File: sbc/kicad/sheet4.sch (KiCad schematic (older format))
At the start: 44 parts, among them SW1 \"D\", SW10 \"4\", SW11 \"5\", SW12 \"6\", SW13 \"1\", SW14 \"2\", SW15 \"3\", SW16 \"0\", SW17 \"RESET\", SW18 SEGMENT TEST, SW2 \"E\", SW3 \"F\", SW4 \"A\", SW5 \"B\", SW6 \"C\", SW7 \"7\", SW8 \"8\", SW9 \"9\", U10 MAN71A, U11 74LS259, U12 74LS259, U13 74LS259, U14 74LS259, U15 74LS259, U16 74LS259, U17 74LS244, U5 MAN71A, U6 MAN71A, U7 MAN71A, U8 MAN71A, U9 MAN71A

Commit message: Updates, start of PCB.
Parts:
- removed SW18: SEGMENT TEST, symbol Switch:SW_Push_45deg
- added J11: SEGMENT TEST, Connector_PinHeader_2.54mm:PinHeader_1x02_P2.54mm_Vertical, symbol Connector:Conn_01x02_Male
- C23: footprint (none) -> Capacitor_THT:CP_Radial_D4.0mm_P2.00mm
- R5: renamed from R53; footprint (none) -> Resistor_THT:R_Axial_DIN0204_L3.6mm_D1.6mm_P7.62mm_Horizontal
- R6: renamed from R54; footprint (none) -> Resistor_THT:R_Axial_DIN0204_L3.6mm_D1.6mm_P7.62mm_Horizontal
- RN1: renamed from RN3; footprint (none) -> Connector_PinHeader_2.54mm:PinHeader_2x08_P2.54mm_Vertical
- RN2: renamed from RN4; footprint (none) -> Connector_PinHeader_2.54mm:PinHeader_2x08_P2.54mm_Vertical
- RN3: renamed from RN5; footprint (none) -> Connector_PinHeader_2.54mm:PinHeader_2x08_P2.54mm_Vertical
- RN4: renamed from RN6; footprint (none) -> Connector_PinHeader_2.54mm:PinHeader_2x08_P2.54mm_Vertical
- RN5: renamed from RN7; footprint (none) -> Connector_PinHeader_2.54mm:PinHeader_2x08_P2.54mm_Vertical
- RN6: renamed from RN8; footprint (none) -> Connector_PinHeader_2.54mm:PinHeader_2x08_P2.54mm_Vertical
- SW10: renamed from SW9; footprint (none) -> Button_Switch_THT:SW_PUSH_6mm_H4.3mm
- SW11: renamed from SW10; footprint (none) -> Button_Switch_THT:SW_PUSH_6mm_H4.3mm
- SW12: renamed from SW11; footprint (none) -> Button_Switch_THT:SW_PUSH_6mm_H4.3mm
- SW13: renamed from SW12; footprint (none) -> Button_Switch_THT:SW_PUSH_6mm_H4.3mm
- SW14: renamed from SW13; footprint (none) -> Button_Switch_THT:SW_PUSH_6mm_H4.3mm
- SW15: renamed from SW14; footprint (none) -> Button_Switch_THT:SW_PUSH_6mm_H4.3mm
- SW16: renamed from SW15; footprint (none) -> Button_Switch_THT:SW_PUSH_6mm_H4.3mm
- SW17: renamed from SW16; footprint (none) -> Button_Switch_THT:SW_PUSH_6mm_H4.3mm
- SW18: renamed from SW17; footprint (none) -> Button_Switch_THT:SW_PUSH_6mm_H4.3mm
- SW2: renamed from SW1; footprint (none) -> Button_Switch_THT:SW_PUSH_6mm_H4.3mm
- SW3: renamed from SW2; footprint (none) -> Button_Switch_THT:SW_PUSH_6mm_H4.3mm
- SW4: renamed from SW3; footprint (none) -> Button_Switch_THT:SW_PUSH_6mm_H4.3mm
- SW5: renamed from SW4; footprint (none) -> Button_Switch_THT:SW_PUSH_6mm_H4.3mm
- SW6: renamed from SW5; footprint (none) -> Button_Switch_THT:SW_PUSH_6mm_H4.3mm
- SW7: renamed from SW6; footprint (none) -> Button_Switch_THT:SW_PUSH_6mm_H4.3mm
- SW8: renamed from SW7; footprint (none) -> Button_Switch_THT:SW_PUSH_6mm_H4.3mm
- SW9: renamed from SW8; footprint (none) -> Button_Switch_THT:SW_PUSH_6mm_H4.3mm
- U12: renamed from U11; footprint (none) -> Package_DIP:DIP-16_W7.62mm_Socket
- U13: renamed from U12; footprint (none) -> Package_DIP:DIP-16_W7.62mm_Socket
- U14: renamed from U13; footprint (none) -> Package_DIP:DIP-16_W7.62mm_Socket
- U15: renamed from U14; footprint (none) -> Package_DIP:DIP-16_W7.62mm_Socket
- U16: renamed from U15; footprint (none) -> Package_DIP:DIP-16_W7.62mm_Socket
- U17: renamed from U16; footprint (none) -> Package_DIP:DIP-16_W7.62mm_Socket
- U18: renamed from U17; footprint (none) -> Package_DIP:DIP-20_W7.62mm_Socket
- renumbered D7 to D10, D5 to D8, D6 to D9, RN1 to RN7, U9 to U10, U10 to U11, U5 to U6, U6 to U7, U7 to U8, U8 to U9
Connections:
- net GND: now also J11.1 (Pin_1)
- net at R5.1, U12.15 (Clr), U13.15 (Clr)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: now also J11.2 (Pin_2)
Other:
- moved on the sheet: R5

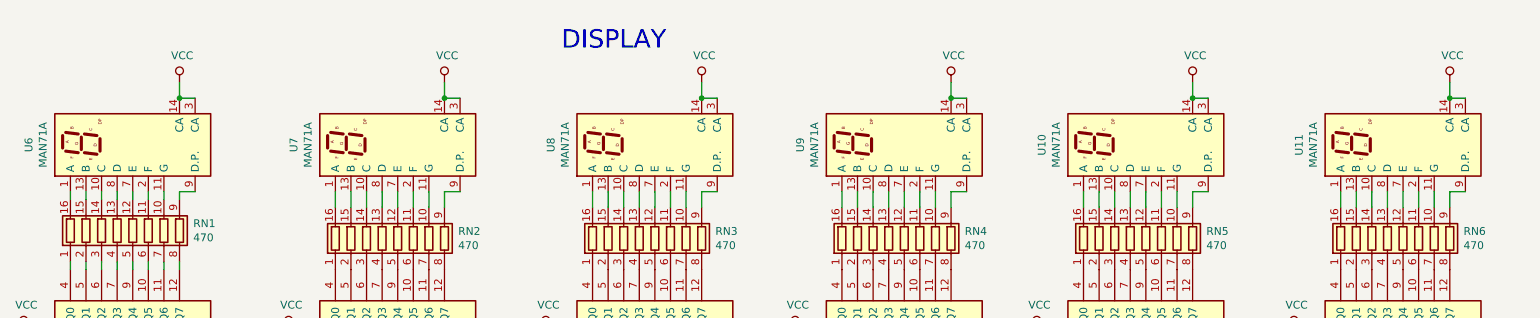
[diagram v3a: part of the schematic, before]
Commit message: Fix error in LED wiring.
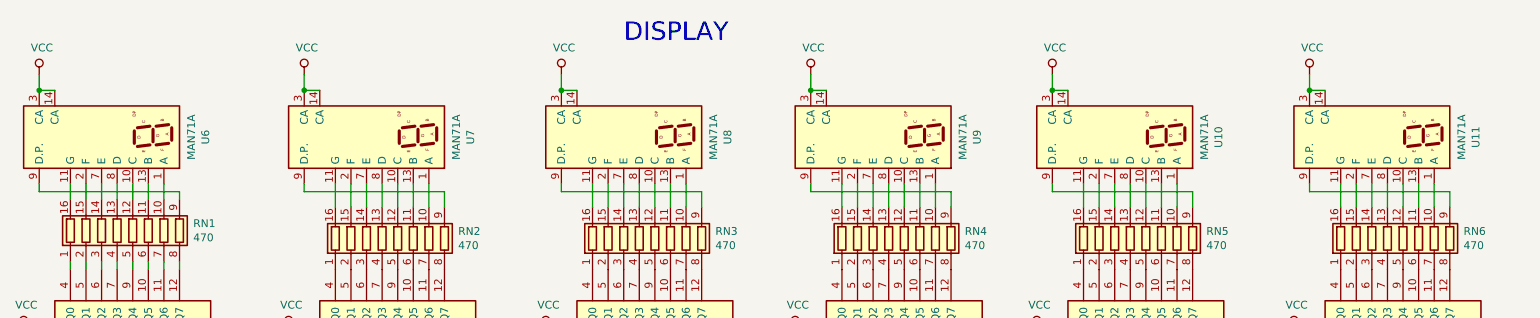
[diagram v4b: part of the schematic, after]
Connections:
- net at U6.1 (A): now also RN1.10 (R7.2); no longer RN1.16 (R1.2)
- net at U6.10 (C): now also RN1.12 (R5.2); no longer RN1.14 (R3.2)
- net at U6.11 (G): now also RN1.16 (R1.2); no longer RN1.10 (R7.2)
- net at U6.13 (B): now also RN1.11 (R6.2); no longer RN1.15 (R2.2)
- net at U6.2 (F): now also RN1.15 (R2.2); no longer RN1.11 (R6.2)
- net at U6.7 (E): now also RN1.14 (R3.2); no longer RN1.12 (R5.2)
- net at RN2.10 (R7.2): now also U7.1 (A); no longer U7.11 (G)
- net at RN2.11 (R6.2): now also U7.13 (B); no longer U7.2 (F)
- net at RN2.12 (R5.2): now also U7.10 (C); no longer U7.7 (E)
- net at RN2.14 (R3.2): now also U7.7 (E); no longer U7.10 (C)
- net at RN2.15 (R2.2): now also U7.2 (F); no longer U7.13 (B)
- net at RN2.16 (R1.2): now also U7.11 (G); no longer U7.1 (A)
- net at RN3.10 (R7.2): now also U8.1 (A); no longer U8.11 (G)
- net at RN3.11 (R6.2): now also U8.13 (B); no longer U8.2 (F)
- net at RN3.12 (R5.2): now also U8.10 (C); no longer U8.7 (E)
- net at RN3.14 (R3.2): now also U8.7 (E); no longer U8.10 (C)
- net at RN3.15 (R2.2): now also U8.2 (F); no longer U8.13 (B)
- net at RN3.16 (R1.2): now also U8.11 (G); no longer U8.1 (A)
- net at RN4.10 (R7.2): now also U9.1 (A); no longer U9.11 (G)
- net at RN4.11 (R6.2): now also U9.13 (B); no longer U9.2 (F)
- net at RN4.12 (R5.2): now also U9.10 (C); no longer U9.7 (E)
- net at RN4.14 (R3.2): now also U9.7 (E); no longer U9.10 (C)
- net at RN4.15 (R2.2): now also U9.2 (F); no longer U9.13 (B)
- net at RN4.16 (R1.2): now also U9.11 (G); no longer U9.1 (A)
- net at RN5.10 (R7.2): now also U10.1 (A); no longer U10.11 (G)
- net at RN5.11 (R6.2): now also U10.13 (B); no longer U10.2 (F)
- net at RN5.12 (R5.2): now also U10.10 (C); no longer U10.7 (E)
- net at RN5.14 (R3.2): now also U10.7 (E); no longer U10.10 (C)
- net at RN5.15 (R2.2): now also U10.2 (F); no longer U10.13 (B)
- net at RN5.16 (R1.2): now also U10.11 (G); no longer U10.1 (A)
- net at RN6.10 (R7.2): now also U11.1 (A); no longer U11.11 (G)
- net at RN6.11 (R6.2): now also U11.13 (B); no longer U11.2 (F)
- net at RN6.12 (R5.2): now also U11.10 (C); no longer U11.7 (E)
- net at RN6.14 (R3.2): now also U11.7 (E); no longer U11.10 (C)
- net at RN6.15 (R2.2): now also U11.2 (F); no longer U11.13 (B)
- net at RN6.16 (R1.2): now also U11.11 (G); no longer U11.1 (A)
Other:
- moved on the sheet: U10, U11, U6, U7, U8, U9

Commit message: Various updates.
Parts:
- removed RN1, RN2, RN3, RN4, RN5, RN6: 470, Connector_PinHeader_2.54mm:PinHeader_2x08_P2.54mm_Vertical, symbol Device:R_Pack08
- added R10, R11, R12, R13, R14, R15, R16, R17, R18, R19, R20, R21, R22, R23, R24, R25, R26, R27, R28, R29, R30, R31, R32, R33, R34, R35, R36, R37, R38, R39, R40, R41, R42, R43, R44, R45, R46, R47, R48, R49, R50, R51, R52, R53, R54, R7, R8, R9: 470, Resistor_THT:R_Axial_DIN0204_L3.6mm_D1.6mm_P7.62mm_Horizontal, symbol Device:R
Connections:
- net at U6.1 (A): now also R13.1
- net at U6.10 (C): now also R11.1
- net at U6.11 (G): now also R7.1
- net at U6.13 (B): now also R12.1
- net at U6.2 (F): now also R8.1
- net at U6.7 (E): now also R9.1
- net at U6.8 (D): now also R10.1
- net at U6.9 (D.P.): now also R14.1
- net at U12.10 (Q5): now also R12.2
- net at U12.11 (Q6): now also R13.2
- net at U12.12 (Q7): now also R14.2
- net at U12.4 (Q0): now also R7.2
- net at U12.5 (Q1): now also R8.2
- net at U12.6 (Q2): now also R9.2
- net at U12.7 (Q3): now also R10.2
- net at U12.9 (Q4): now also R11.2
- net at U13.4 (Q0): now also R15.2
- net at U7.1 (A): now also R21.1
- net at U7.13 (B): now also R20.1
- net at U7.10 (C): now also R19.1
- net at U7.8 (D): now also R18.1
- net at U7.7 (E): now also R17.1
- net at U7.2 (F): now also R16.1
- net at U7.11 (G): now also R15.1
- net at U13.5 (Q1): now also R16.2
- net at U13.6 (Q2): now also R17.2
- net at U13.7 (Q3): now also R18.2
- net at U13.9 (Q4): now also R19.2
- net at U13.10 (Q5): now also R20.2
- net at U13.11 (Q6): now also R21.2
- net at U13.12 (Q7): now also R22.2
- net at U7.9 (D.P.): now also R22.1
- net at U14.4 (Q0): now also R23.2
- net at U8.1 (A): now also R29.1
- net at U8.13 (B): now also R28.1
- net at U8.10 (C): now also R27.1
- net at U8.8 (D): now also R26.1
- net at U8.7 (E): now also R25.1
- net at U8.2 (F): now also R24.1
- net at U8.11 (G): now also R23.1
- net at U14.5 (Q1): now also R24.2
- net at U14.6 (Q2): now also R25.2
- net at U14.7 (Q3): now also R26.2
- net at U14.9 (Q4): now also R27.2
- net at U14.10 (Q5): now also R28.2
- net at U14.11 (Q6): now also R29.2
- net at U14.12 (Q7): now also R30.2
- net at U8.9 (D.P.): now also R30.1
- net at U15.4 (Q0): now also R31.2
- net at U9.1 (A): now also R37.1
- net at U9.13 (B): now also R36.1
- net at U9.10 (C): now also R35.1
- net at U9.8 (D): now also R34.1
- net at U9.7 (E): now also R33.1
- net at U9.2 (F): now also R32.1
- net at U9.11 (G): now also R31.1
- net at U15.5 (Q1): now also R32.2
- net at U15.6 (Q2): now also R33.2
- net at U15.7 (Q3): now also R34.2
- net at U15.9 (Q4): now also R35.2
- net at U15.10 (Q5): now also R36.2
- net at U15.11 (Q6): now also R37.2
- net at U15.12 (Q7): now also R38.2
- net at U9.9 (D.P.): now also R38.1
- net at U16.4 (Q0): now also R39.2
- net at U10.1 (A): now also R45.1
- net at U10.13 (B): now also R44.1
- net at U10.10 (C): now also R43.1
- net at U10.8 (D): now also R42.1
- net at U10.7 (E): now also R41.1
- net at U10.2 (F): now also R40.1
- net at U10.11 (G): now also R39.1
- net at U16.5 (Q1): now also R40.2
- net at U16.6 (Q2): now also R41.2
- net at U16.7 (Q3): now also R42.2
- net at U16.9 (Q4): now also R43.2
- net at U16.10 (Q5): now also R44.2
- net at U16.11 (Q6): now also R45.2
- net at U16.12 (Q7): now also R46.2
- net at U10.9 (D.P.): now also R46.1
- net at U17.4 (Q0): now also R47.2
- net at U11.1 (A): now also R53.1
- net at U11.13 (B): now also R52.1
- net at U11.10 (C): now also R51.1
- net at U11.8 (D): now also R50.1
- net at U11.7 (E): now also R49.1
- net at U11.2 (F): now also R48.1
- net at U11.11 (G): now also R47.1
- net at U17.5 (Q1): now also R48.2
- net at U17.6 (Q2): now also R49.2
- net at U17.7 (Q3): now also R50.2
- net at U17.9 (Q4): now also R51.2
- net at U17.10 (Q5): now also R52.2
- net at U17.11 (Q6): now also R53.2
- net at U17.12 (Q7): now also R54.2
- net at U11.9 (D.P.): now also R54.1

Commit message: Getting close to ready to order PCBs. Check in all files.
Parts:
- removed RN7: 8K2, Resistor_THT:R_Array_SIP7, symbol Device:R_Network06
- added R55, R56, R57, R58, R59, R60: 8K2, Resistor_THT:R_Axial_DIN0204_L3.6mm_D1.6mm_P7.62mm_Horizontal, symbol Device:R
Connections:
- net VCC: now also R55.1, R56.1, R57.1, R58.1, R59.1, R60.1
- net at U18.11 (I0b): now also R56.2
- net at SW17.2, U18.13 (I1b): now also R55.2
- net at SW2.2, SW3.2, SW4.2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: now also R60.2
- net at U18.4 (I1a): now also R59.2
- net at U18.6 (I2a): now also R58.2
- net at U18.8 (I3a): now also R57.2
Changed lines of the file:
@@
 Sheet 4 6
 Title "6800 SIngle Board Computer"
-Date "2022-02-09"
+Date "2022-02-12"
 Rev "0.1"
 Comp "Jeff Tranter"
@@
 Wire Wire Line
 	3400 6750 3400 5900
-$Comp
-L Device:R_Network06 RN7
-U 1 1 623FE313
-P 3400 5050
-F 0 "RN7" H 3300 5250 50  0000 C CNN
-F 1 "8K2" H 3550 5250 50  0000 C CNN
-F 2 "Resistor_THT:R_Array_SIP7" V 3775 5050 50  0001 C CNN
-F 3 "http://www.vishay.com/docs/31509/csc.pdf" H 3400 5050 50  0001 C CNN
-	1    3400 5050
-	1    0    0    -1
-$EndComp
 Wire Wire Line
 	3600 5250 3600 5400
@@
 	1    0    0    -1
 $EndComp
-Wire Wire Line
-	3100 4850 3100 4750
 Text GLabel 3900 4600 1    50   Input ~ 0
 A0
@@
 Wire Wire Line
 	4450 6750 4450 6850
-$Comp
-L Device:R R6
-U 1 1 6257E9F5
-P 5150 7100
-F 0 "R6" H 5220 7146 50  0000 L CNN
-F 1 "3K" H 5220 7055 50  0000 L CNN
-F 2 "Resistor_THT:R_Axial_DIN0204_L3.6mm_D1.6mm_P7.62mm_Horizontal" V 5080 7100 50  0001 C CNN
-F 3 "~" H 5150 7100 50  0001 C CNN
-	1    5150 7100
-	1    0    0    -1
-$EndComp
 $Comp
 L power:VCC #PWR047
@@
 Wire Wire Line
 	5150 1700 5150 1850
+$Comp
+L Device:R R6
+U 1 1 6257E9F5
+P 5150 7100
+F 0 "R6" H 5220 7146 50  0000 L CNN
+F 1 "3K" H 5220 7055 50  0000 L CNN
+F 2 "Resistor_THT:R_Axial_DIN0204_L3.6mm_D1.6mm_P7.62mm_Horizontal" V 5080 7100 50  0001 C CNN
+F 3 "~" H 5150 7100 50  0001 C CNN
+	1    5150 7100
+	1    0    0    -1
+$EndComp
+$Comp
+L Device:R R55
+U 1 1 620A360E
+P 3100 5100
+F 0 "R55" H 3050 5300 50  0000 L CNN
+F 1 "8K2" H 3050 4950 50  0000 L CNN
+F 2 "Resistor_THT:R_Axial_DIN0204_L3.6mm_D1.6mm_P7.62mm_Horizontal" V 3030 5100 50  0001 C CNN
+F 3 "~" H 3100 5100 50  0001 C CNN
+	1    3100 5100
+	1    0    0    -1
+$EndComp
+$Comp
+L Device:R R56
+U 1 1 620A46F1
+P 3200 5100
+F 0 "R56" H 3150 5350 50  0000 L CNN
+F 1 "8K2" H 3150 4900 50  0000 L CNN
+F 2 "Resistor_THT:R_Axial_DIN0204_L3.6mm_D1.6mm_P7.62mm_Horizontal" V 3130 5100 50  0001 C CNN
+F 3 "~" H 3200 5100 50  0001 C CNN
+	1    3200 5100
+	1    0    0    -1
+$EndComp
+$Comp
+L Device:R R57
+U 1 1 620A4865
+P 3300 5100
+F 0 "R57" H 3250 5300 50  0000 L CNN
+F 1 "8K2" H 3250 4950 50  0000 L CNN
+F 2 "Resistor_THT:R_Axial_DIN0204_L3.6mm_D1.6mm_P7.62mm_Horizontal" V 3230 5100 50  0001 C CNN
+F 3 "~" H 3300 5100 50  0001 C CNN
+	1    3300 5100
+	1    0    0    -1
+$EndComp
+$Comp
+L Device:R R58
+U 1 1 620A4AA0
+P 3400 5100
+F 0 "R58" H 3350 5350 50  0000 L CNN
+F 1 "8K2" H 3350 4900 50  0000 L CNN
+F 2 "Resistor_THT:R_Axial_DIN0204_L3.6mm_D1.6mm_P7.62mm_Horizontal" V 3330 5100 50  0001 C CNN
+F 3 "~" H 3400 5100 50  0001 C CNN
+	1    3400 5100
+	1    0    0    -1
+$EndComp
+$Comp
+L Device:R R60
+U 1 1 620A4C34
+P 3600 5100
+F 0 "R60" H 3550 5350 50  0000 L CNN
+F 1 "8K2" H 3550 4900 50  0000 L CNN
+F 2 "Resistor_THT:R_Axial_DIN0204_L3.6mm_D1.6mm_P7.62mm_Horizontal" V 3530 5100 50  0001 C CNN
+F 3 "~" H 3600 5100 50  0001 C CNN
+	1    3600 5100
+	1    0    0    -1
+$EndComp
+$Comp
+L Device:R R59
+U 1 1 620A4E16
+P 3500 5100
+F 0 "R59" H 3450 5300 50  0000 L CNN
+F 1 "8K2" H 3450 4950 50  0000 L CNN
+F 2 "Resistor_THT:R_Axial_DIN0204_L3.6mm_D1.6mm_P7.62mm_Horizontal" V 3430 5100 50  0001 C CNN
+F 3 "~" H 3500 5100 50  0001 C CNN
+	1    3500 5100
+	1    0    0    -1
+$EndComp
+Wire Wire Line
+	3600 4950 3500 4950
+Wire Wire Line
+	3400 4950 3300 4950
+Wire Wire Line
+	3200 4950 3100 4950
+Wire Wire Line
+	3100 4750 3100 4950
+Connection ~ 3100 4950
+Wire Wire Line
+	3200 4950 3300 4950
+Connection ~ 3200 4950
+Connection ~ 3300 4950
+Wire Wire Line
+	3400 4950 3500 4950
+Connection ~ 3400 4950
+Connection ~ 3500 4950
 $EndSCHEMATC

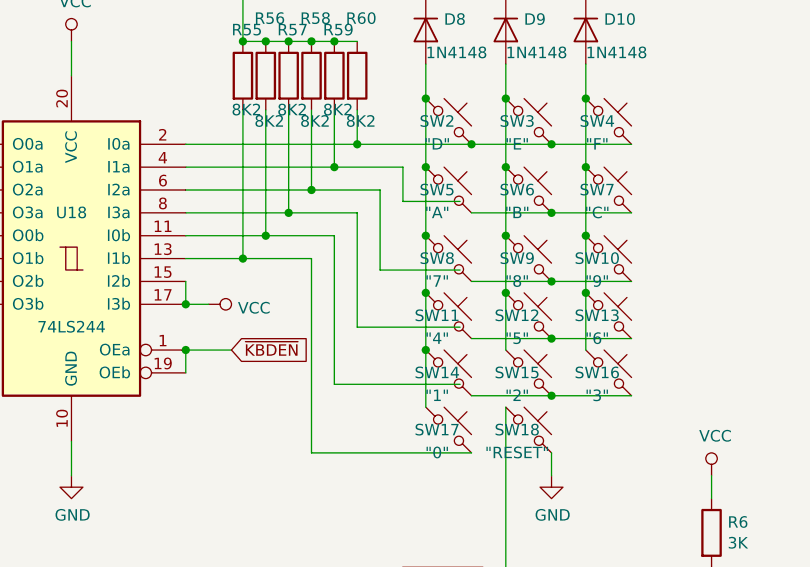
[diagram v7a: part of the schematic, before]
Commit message: Some corrections to schematic and added to documentation.
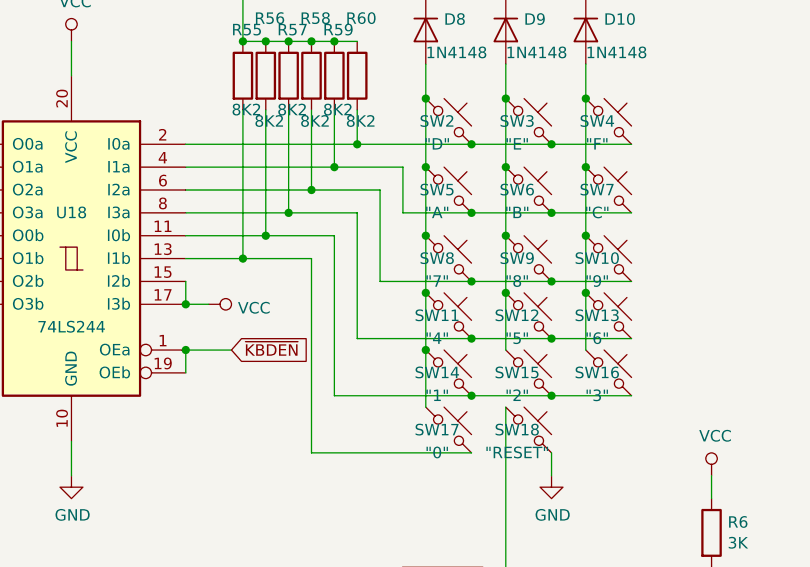
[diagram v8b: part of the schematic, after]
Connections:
- net at R56.2, U18.11 (I0b): now also SW14.2, SW15.2, SW16.2
- net at R59.2, U18.4 (I1a): now also SW5.2, SW6.2, SW7.2
- net at R58.2, U18.6 (I2a): now also SW10.2, SW8.2, SW9.2
- net at R57.2, U18.8 (I3a): now also SW11.2, SW12.2, SW13.2
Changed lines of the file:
@@
 Sheet 4 6
 Title "6800 SIngle Board Computer"
-Date "2022-02-12"
+Date "2022-03-02"
 Rev "0.1"
 Comp "Jeff Tranter"
@@
 Connection ~ 4100 5400
 Wire Wire Line
-	4050 5650 3800 5650
-Wire Wire Line
-	3800 5650 3800 5500
-Wire Wire Line
 	3800 5500 3500 5500
 Wire Wire Line
-	4050 5950 3700 5950
-Wire Wire Line
-	3700 5950 3700 5600
-Wire Wire Line
 	3700 5600 3400 5600
 Wire Wire Line
-	4050 6200 3600 6200
-Wire Wire Line
-	3600 6200 3600 5700
-Wire Wire Line
 	3600 5700 3300 5700
-Wire Wire Line
-	4050 6450 3500 6450
-Wire Wire Line
-	3500 6450 3500 5800
 Wire Wire Line
 	4100 6750 3400 6750
@@
 Connection ~ 3400 4950
 Connection ~ 3500 4950
+Wire Wire Line
+	3800 5500 3800 5700
+Wire Wire Line
+	3800 5700 4100 5700
+Connection ~ 4100 5700
+Wire Wire Line
+	3700 5600 3700 6000
+Wire Wire Line
+	3700 6000 4100 6000
+Connection ~ 4100 6000
+Wire Wire Line
+	3600 5700 3600 6250
+Wire Wire Line
+	3600 6250 4100 6250
+Connection ~ 4100 6250
+Wire Wire Line
+	3500 6500 4100 6500
+Connection ~ 4100 6500
+Wire Wire Line
+	3500 5800 3500 6500
 $EndSCHEMATC
